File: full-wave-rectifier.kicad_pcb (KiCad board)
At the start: 2 copper layers, 80.6 x 108 mm, 64 parts, among them J10 Control Right, J11 Main Right, J12 Power Connector, J2 Input Ch1, J3 Input Ch2, J4 Output Ch1, J5 Output Ch2, J6 Ochd input, J8 Control Left, J9 Main Left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

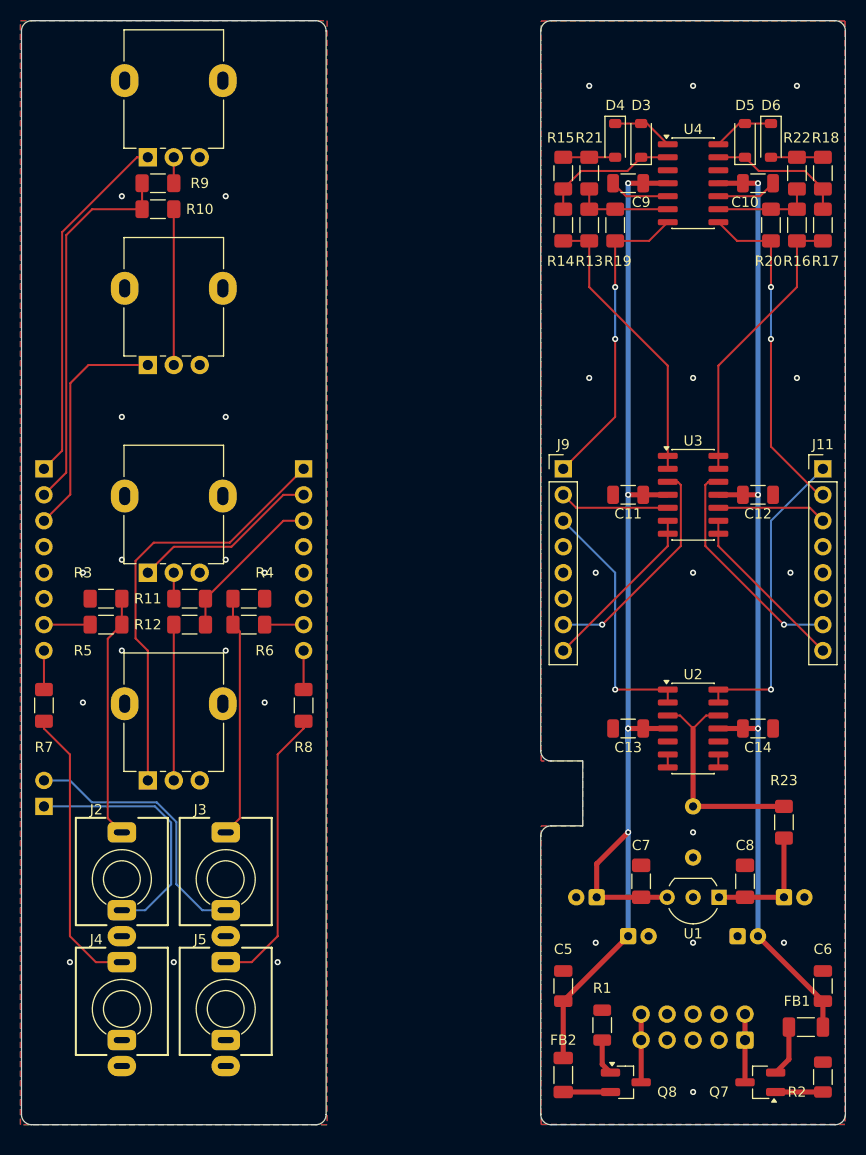
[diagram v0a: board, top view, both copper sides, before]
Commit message: Sync sizes of both modules
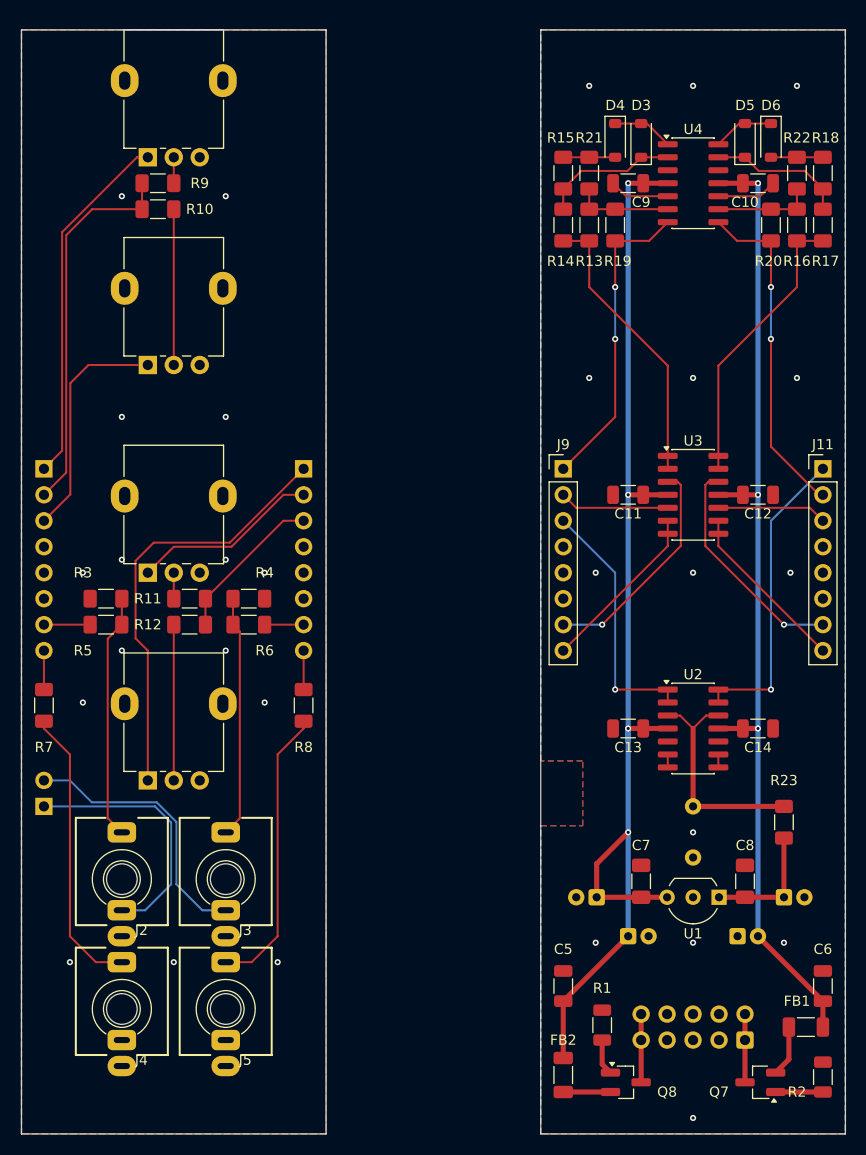
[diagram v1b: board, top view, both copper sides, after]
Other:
- outline, holes or cut-outs redrawn

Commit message: save changes
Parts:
- D3, D4, D5, D6: footprint Diode_SMD:D_SOD-123 -> Eurorack:D_SOD-123_Metric1.30x1.75mm_HandSolder
- moved J12 2.54 mm to (182.9, 149.9)
- moved Q7 2.54 mm to (184.4, 154.0)
- moved Q8 2.54 mm to (171.2, 154.0)
- moved R1 2.54 mm to (168.9, 148.4)
- moved C1 2.54 mm to (171.4, 139.7)
- moved C2 2.54 mm to (182.2, 139.7)
- moved C5 2.54 mm to (165.1, 144.6)
- moved C6 2.54 mm to (190.5, 144.6)
- moved FB1 2.54 mm to (188.8, 148.6)
- moved FB2 2.54 mm to (165.1, 153.3)
- moved R2 2.54 mm to (190.5, 153.5)
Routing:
- net +12V: track 116.9 -> 119.4 mm
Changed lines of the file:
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@@
 	(footprint "Inductor_SMD:L_1206_3216Metric_Pad1.22x1.90mm_HandSolder"
 		(layer "F.Cu")
-		(at 188.8375 146.05 180)
+		(at 188.8375 148.59 180)
 		(descr "Inductor SMD 1206 (3216 Metric), square (rectangular) end terminal, IPC-7351 nominal with elongated pad for handsoldering. (Body size source: IPC-SM-782 page 80, https://www.pcb-3d.com/wordpress/wp-content/uploads/ipc-sm-782a_amendment_1_and_2.pdf), generated with kicad-footprint-generator")
 		(tags "inductor handsolder")
@@
 	(footprint "Resistor_SMD:R_1206_3216Metric"
 		(layer "F.Cu")
-		(at 168.91 145.8575 90)
+		(at 168.91 148.3975 90)
 		(descr "Resistor SMD 1206 (3216 Metric), square (rectangular) end terminal, IPC-7351 nominal, (Body size source: IPC-SM-782 page 72, https://www.pcb-3d.com/wordpress/wp-content/uploads/ipc-sm-782a_amendment_1_and_2.pdf), generated with kicad-footprint-generator")
 		(tags "resistor")
@@
 	(footprint "Resistor_SMD:R_1206_3216Metric"
 		(layer "F.Cu")
-		(at 190.5 150.9375 90)
+		(at 190.5 153.4775 90)
 		(descr "Resistor SMD 1206 (3216 Metric), square (rectangular) end terminal, IPC-7351 nominal, (Body size source: IPC-SM-782 page 72, https://www.pcb-3d.com/wordpress/wp-content/uploads/ipc-sm-782a_amendment_1_and_2.pdf), generated with kicad-footprint-generator")
 		(tags "resistor")
@@
 		)
 	)
-	(footprint "Diode_SMD:D_SOD-123"
+	(footprint "Eurorack:D_SOD-123_Metric1.30x1.75mm_HandSolder"
 		(layer "F.Cu")
 		(at 182.88 59.31 90)
@@
 		(pad "1" smd roundrect
 			(at -1.65 0 90)
-			(size 0.9 1.2)
+			(size 1.3 1.75)
 			(layers "F.Cu" "F.Mask" "F.Paste")
 			(roundrect_rratio 0.25)
@@
 		(pad "2" smd roundrect
 			(at 1.65 0 90)
-			(size 0.9 1.2)
+			(size 1.3 1.75)
 			(layers "F.Cu" "F.Mask" "F.Paste")
 			(roundrect_rratio 0.25)
@@
 	(footprint "Package_TO_SOT_SMD:SOT-23_Handsoldering"
 		(layer "F.Cu")
-		(at 171.22 151.45)
+		(at 171.22 153.99)
 		(descr "SOT-23, Handsoldering")
 		(tags "SOT-23")
@@
 	(footprint "Package_TO_SOT_SMD:SOT-23_Handsoldering"
 		(layer "F.Cu")
-		(at 184.38 151.45 180)
+		(at 184.38 153.99 180)
 		(descr "SOT-23, Handsoldering")
 		(tags "SOT-23")
@@
 	(footprint "Capacitor_SMD:C_1206_3216Metric"
 		(layer "F.Cu")
-		(at 190.5 142.035 -90)
+		(at 190.5 144.575 -90)
 		(descr "Capacitor SMD 1206 (3216 Metric), square (rectangular) end terminal, IPC-7351 nominal, (Body size source: IPC-SM-782 page 76, https://www.pcb-3d.com/wordpress/wp-content/uploads/ipc-sm-782a_amendment_1_and_2.pdf), generated with kicad-footprint-generator")
 		(tags "capacitor")
@@
 		)
 	)
-	(footprint "Diode_SMD:D_SOD-123"
+	(footprint "Eurorack:D_SOD-123_Metric1.30x1.75mm_HandSolder"
 		(layer "F.Cu")
 		(at 170.18 59.31 -90)
@@
 		(tags "SOD-123")
 		(property "Reference" "D4"
-			(at -3.43 0 0)
+			(at -3.43 0 180)
 			(layer "F.SilkS")
 			(effects
@@
 		)
 		(property "Value" "1N4148"
-			(at 0 2.1 90)
+			(at 0 2.1 270)
 			(layer "F.Fab")
 			(effects
@@
 		)
 		(fp_text user "${REFERENCE}"
-			(at 0 -2 90)
+			(at 0 -2 270)
 			(layer "F.Fab")
 			(effects
@@
 		(pad "1" smd roundrect
 			(at -1.65 0 270)
-			(size 0.9 1.2)
+			(size 1.3 1.75)
 			(layers "F.Cu" "F.Mask" "F.Paste")
 			(roundrect_rratio 0.25)
@@
 		(pad "2" smd roundrect
 			(at 1.65 0 270)
-			(size 0.9 1.2)
+			(size 1.3 1.75)
 			(layers "F.Cu" "F.Mask" "F.Paste")
 			(roundrect_rratio 0.25)
@@
 		)
 	)
-	(footprint "Diode_SMD:D_SOD-123"
+	(footprint "Eurorack:D_SOD-123_Metric1.30x1.75mm_HandSolder"
 		(layer "F.Cu")
 		(at 172.72 59.31 90)
@@
 		(pad "1" smd roundrect
 			(at -1.65 0 90)
-			(size 0.9 1.2)
+			(size 1.3 1.75)
 			(layers "F.Cu" "F.Mask" "F.Paste")
 			(roundrect_rratio 0.25)
@@
 		(pad "2" smd roundrect
 			(at 1.65 0 90)
-			(size 0.9 1.2)
+			(size 1.3 1.75)
 			(layers "F.Cu" "F.Mask" "F.Paste")
 			(roundrect_rratio 0.25)
@@
 	(footprint "Inductor_SMD:L_1206_3216Metric_Pad1.22x1.90mm_HandSolder"
 		(layer "F.Cu")
-		(at 165.1 150.7375 -90)
+		(at 165.1 153.2775 -90)
 		(descr "Inductor SMD 1206 (3216 Metric), square (rectangular) end terminal, IPC-7351 nominal with elongated pad for handsoldering. (Body size source: IPC-SM-782 page 80, https://www.pcb-3d.com/wordpress/wp-content/uploads/ipc-sm-782a_amendment_1_and_2.pdf), generated with kicad-footprint-generator")
 		(tags "inductor handsolder")
@@
 		)
 	)
-	(footprint "Diode_SMD:D_SOD-123"
+	(footprint "Eurorack:D_SOD-123_Metric1.30x1.75mm_HandSolder"
 		(layer "F.Cu")
 		(at 185.42 59.31 -90)
@@
 		)
 		(property "Value" "1N4148"
-			(at 0 2.1 90)
+			(at 0 2.1 270)
 			(layer "F.Fab")
 			(effects
@@
 		)
 		(fp_text user "${REFERENCE}"
-			(at 0 -2 90)
+			(at 0 -2 270)
 			(layer "F.Fab")
 			(effects
@@
 		(pad "1" smd roundrect
 			(at -1.65 0 270)
-			(size 0.9 1.2)
+			(size 1.3 1.75)
 			(layers "F.Cu" "F.Mask" "F.Paste")
 			(roundrect_rratio 0.25)
@@
 		(pad "2" smd roundrect
 			(at 1.65 0 270)
-			(size 0.9 1.2)
+			(size 1.3 1.75)
 			(layers "F.Cu" "F.Mask" "F.Paste")
 			(roundrect_rratio 0.25)
@@
 	(footprint "Capacitor_SMD:C_1206_3216Metric"
 		(layer "F.Cu")
-		(at 165.1 142.035 90)
+		(at 165.1 144.575 90)
 		(descr "Capacitor SMD 1206 (3216 Metric), square (rectangular) end terminal, IPC-7351 nominal, (Body size source: IPC-SM-782 page 76, https://www.pcb-3d.com/wordpress/wp-content/uploads/ipc-sm-782a_amendment_1_and_2.pdf), generated with kicad-footprint-generator")
 		(tags "capacitor")
@@
 	(footprint "Capacitor_THT:CP_Radial_D5.0mm_P2.00mm"
 		(layer "B.Cu")
-		(at 182.15 137.16)
+		(at 182.15 139.7)
 		(descr "CP, Radial series, Radial, pin pitch=2.00mm, diameter=5mm, height=7mm, Electrolytic Capacitor")
 		(tags "CP Radial series Radial pin pitch 2.00mm diameter 5mm height 7mm Electrolytic Capacitor")
@@
 	(footprint "Capacitor_THT:CP_Radial_D5.0mm_P2.00mm"
 		(layer "B.Cu")
-		(at 171.45 137.16)
+		(at 171.45 139.7)
 		(descr "CP, Radial series, Radial, pin pitch=2.00mm, diameter=5mm, height=7mm, Electrolytic Capacitor")
 		(tags "CP Radial series Radial pin pitch 2.00mm diameter 5mm height 7mm Electrolytic Capacitor")
@@
 	(footprint "Connector_IDC:IDC-Header_2x05_P2.54mm_Vertical"
 		(layer "B.Cu")
-		(at 182.88 147.32 90)
+		(at 182.88 149.86 90)
 		(descr "Through hole IDC box header, 2x05, 2.54mm pitch, DIN 41651 / IEC 60603-13, double rows, https://docs.google.com/spreadsheets/d/16SsEcesNF15N3Lb4niX7dcUr-NY5_MFPQhobNuNppn4/edit#gid=0")
 		(tags "Through hole vertical IDC box header THT 2x05 2.54mm double row")
 		(property "Reference" "J12"
-			(at 7.62 -5.08 0)
+			(at -5.08 -5.08 0)
 			(layer "B.SilkS")
 			(effects
@@
 	)
 	(segment
-		(start 168.37 130.08)
-		(end 168.37 133.35)
+		(start 165.1 151.615)
+		(end 165.1 146.05)
 		(width 0.5)
 		(layer "F.Cu")
@@
 	)
 	(segment
-		(start 172.925 116.84)
-		(end 171.45 116.84)
+		(start 168.37 130.08)
+		(end 168.37 133.35)
 		(width 0.5)
 		(layer "F.Cu")
@@
 	)
 	(segment
-		(start 171.45 137.16)
-		(end 165.1 143.51)
+		(start 172.925 116.84)
+		(end 171.45 116.84)
 		(width 0.5)
 		(layer "F.Cu")
@@
 	)
 	(segment
-		(start 165.1 143.51)
-		(end 165.1 149.075)
-		(width 0.5)
-		(layer "F.Cu")
-		(net 2)
-	)
-	(segment
 		(start 172.925 93.98)
 		(end 175.325 93.98)
@@
 	)
 	(segment
+		(start 171.45 139.7)
+		(end 165.1 146.05)
+		(width 0.5)
+		(layer "F.Cu")
+		(net 2)
+	)
+	(segment
 		(start 171.45 93.98)
 		(end 172.925 93.98)
@@
 	)
 	(segment
-		(start 171.45 137.16)
+		(start 171.45 139.7)
 		(end 171.45 127)
 		(width 0.5)
@@
 	)
 	(segment
-		(start 184.15 137.16)
-		(end 190.5 143.51)
-		(width 0.5)
-		(layer "F.Cu")
-		(net 3)
-	)
-	(segment
-		(start 190.5 143.51)
+		(start 184.15 139.7)
 		(end 190.5 146.05)
 		(width 0.5)
@@
 	)
 	(segment
-		(start 184.15 137.16)
-		(end 184.15 116.84)
+		(start 184.15 93.98)
+		(end 184.15 63.5)
 		(width 0.5)
 		(layer "B.Cu")
@@
 	)
 	(segment
-		(start 184.15 93.98)
-		(end 184.15 63.5)
+		(start 184.15 116.84)
+		(end 184.15 93.98)
 		(width 0.5)
 		(layer "B.Cu")
@@
 	)
 	(segment
-		(start 184.15 116.84)
-		(end 184.15 93.98)
+		(start 184.15 139.7)
+		(end 184.15 116.84)
 		(width 0.5)
 		(layer "B.Cu")
@@
 	)
 	(segment
-		(start 187.175 149.205)
-		(end 185.88 150.5)
+		(start 185.88 153.04)
+		(end 187.175 151.745)
 		(width 0.5)
 		(layer "F.Cu")
@@
 	)
 	(segment
-		(start 187.175 146.05)
-		(end 187.175 149.205)
+		(start 187.175 151.745)
+		(end 187.175 148.59)
 		(width 0.5)
 		(layer "F.Cu")
@@
 	)
 	(segment
-		(start 165.1 152.4)
-		(end 169.72 152.4)
+		(start 169.72 154.94)
+		(end 165.1 154.94)
 		(width 0.5)
 		(layer "F.Cu")
@@
 	)
 	(segment
-		(start 172.72 151.45)
-		(end 172.72 147.32)
+		(start 172.72 149.86)
+		(end 172.72 153.99)
 		(width 0.5)
 		(layer "F.Cu")
@@
 	)
 	(segment
-		(start 172.72 144.78)
-		(end 172.72 147.32)
+		(start 172.72 147.32)
+		(end 172.72 149.86)
 		(width 0.5)
 		(layer "F.Cu")
@@
 	)
 	(segment
-		(start 182.88 144.78)
-		(end 182.88 147.32)
+		(start 182.88 147.32)
+		(end 182.88 149.86)
 		(width 0.5)
 		(layer "F.Cu")
@@
 	)
 	(segment
-		(start 182.88 147.32)
-		(end 182.88 151.45)
+		(start 182.88 149.86)
+		(end 182.88 153.99)
 		(width 0.5)
 		(layer "F.Cu")
@@
 	)
 	(segment
-		(start 185.88 152.4)
-		(end 190.5 152.4)
+		(start 185.88 154.94)
+		(end 190.5 154.94)
 		(width 0.5)
 		(layer "F.Cu")
@@
 	)
 	(segment
-		(start 168.91 149.69)
-		(end 169.72 150.5)
+		(start 168.91 149.86)
+		(end 168.91 152.23)
 		(width 0.5)
 		(layer "F.Cu")
@@
 	)
 	(segment
-		(start 168.91 147.32)
-		(end 168.91 149.69)
+		(start 168.91 152.23)
+		(end 169.72 153.04)
 		(width 0.5)
 		(layer "F.Cu")

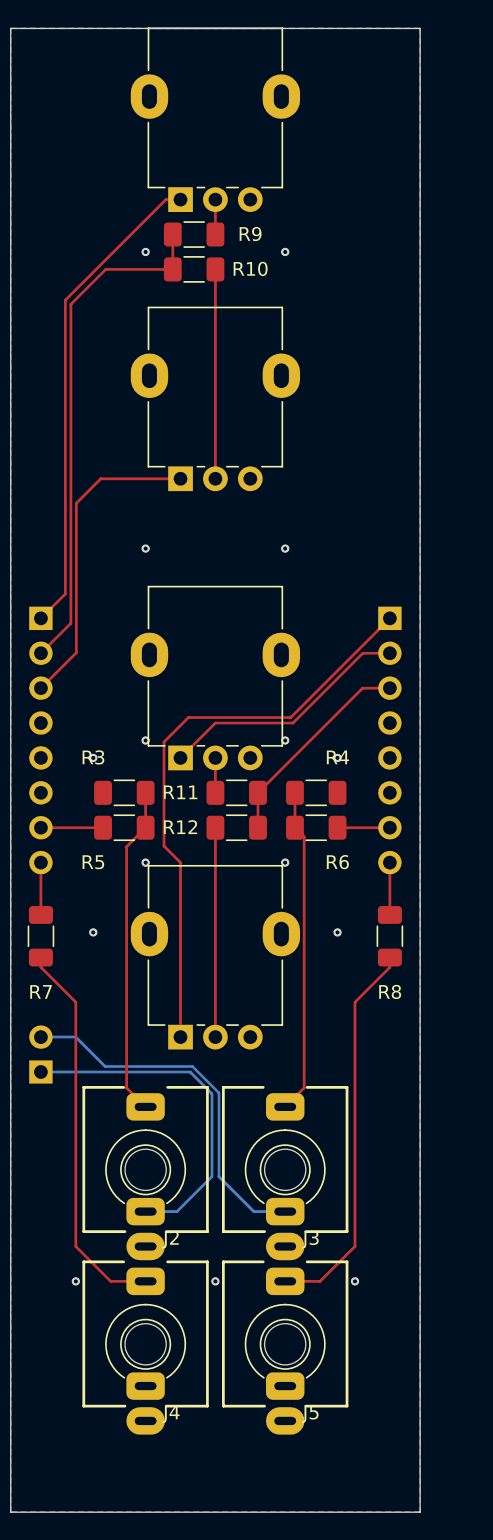
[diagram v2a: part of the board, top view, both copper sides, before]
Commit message: Updated footprint elements
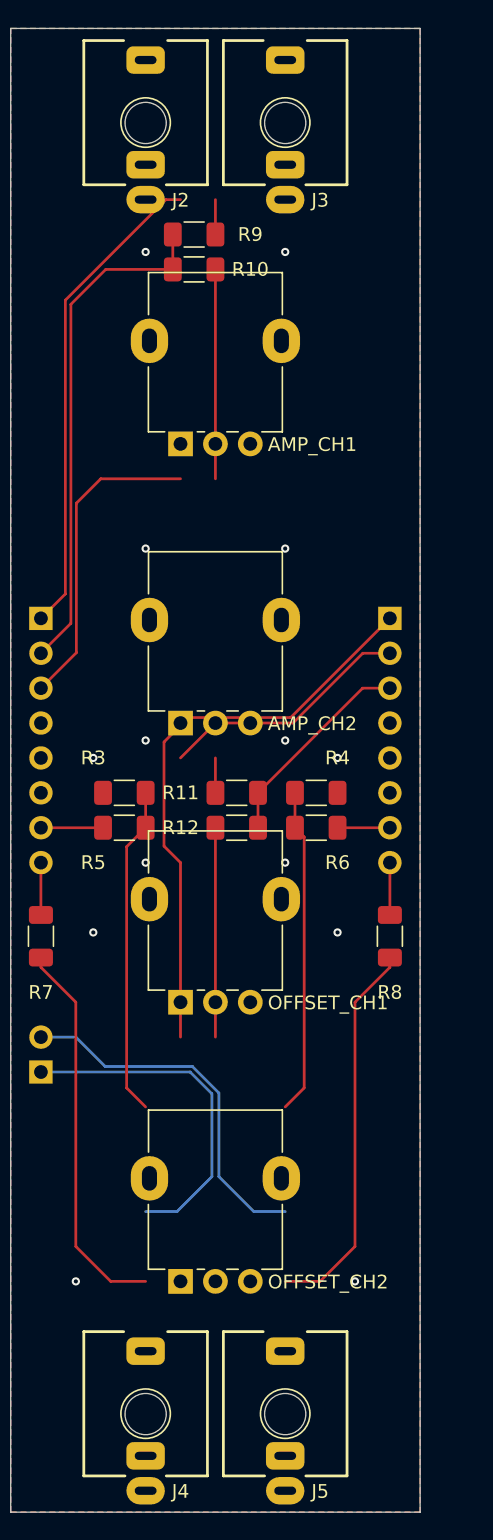
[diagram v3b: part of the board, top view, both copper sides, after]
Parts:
- moved J2 76.2 mm to (121.9, 58.4)
- moved J3 76.2 mm to (132.1, 58.4)
- moved OFFSET_CH1 38.1 mm to (127.0, 119.4)
- moved AMP_CH1 17.8 mm to (127.0, 78.7)
- moved OFFSET_CH2 17.8 mm to (127.0, 139.7)
- moved J4 5.08 mm to (121.9, 152.4)
- moved J5 5.08 mm to (132.1, 152.4)
- moved AMP_CH2 2.54 mm to (127.0, 99.1)
